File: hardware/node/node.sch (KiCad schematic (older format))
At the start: 66 parts, among them J1 BOOT0_Jumper, J2 FTDI, J3 SMA Female, J4 BATTERIES, J5 SWD, Q1 Si2323DDS, SW1 TVCM04N016BB, U1 RFM69HCW, U2 SHTC3, U3 AT25DF512C, U4 STM32L031K6Tx, U5 SN74LVC1T45DBV, U6 SN74LVC1T45DBV, Y1 32.768K-CFPX217

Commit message: Removed UART level translation
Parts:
- removed C10, C11, C8, C9: 100n, Capacitor_SMD:C_0805_2012Metric_Pad1.15x1.40mm_HandSolder, symbol Device:C
- removed R22, R27: 0, Resistor_SMD:R_0805_2012Metric_Pad1.15x1.40mm_HandSolder, symbol Device:R
- removed R23, R24, R26: 100k, Resistor_SMD:R_0805_2012Metric_Pad1.15x1.40mm_HandSolder, symbol Device:R
- removed R28, R29: 330, Resistor_SMD:R_0805_2012Metric_Pad1.15x1.40mm_HandSolder, symbol Device:R
- removed U5, U6: SN74LVC1T45DBV, Package_TO_SOT_SMD:SOT-23-6, symbol Logic_LevelTranslator:SN74LVC1T45DBV
- R11, R12, R14, R16: value 0 -> 330
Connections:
- net labels removed: FTDI_RX, FTDI_TX, FTDI_VCC
- wire segments 310 -> 248
- no-connect marks 9 -> 10
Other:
- note added: "FT232R (used in FTDI cable)\nhas a input switching voltage \nof max 1.5V so it should be \nfine to drive it directly at \neg 2.4 V"
- note added: "PA3 (USART2_RX) is 5V tolerant\nso it should be safe to connect\nit directly to 3.3V FTDI cable"
- note added: "Populate only\none set of \nresistors"
- note removed: "FT232R (used in FTDI cable) has a input switching voltage of max 1.5V\nso it should be fine to drive it directly at eg 2.4 V"
- note removed: "PA3 (USART2_RX) is 5V tolerant so it should \nbe safe to bypass level conversion"
- note removed: "Populate only\none set of resistors"
- note removed: "Power-off leakage current 2uA max"
- note removed: "UART level translation"

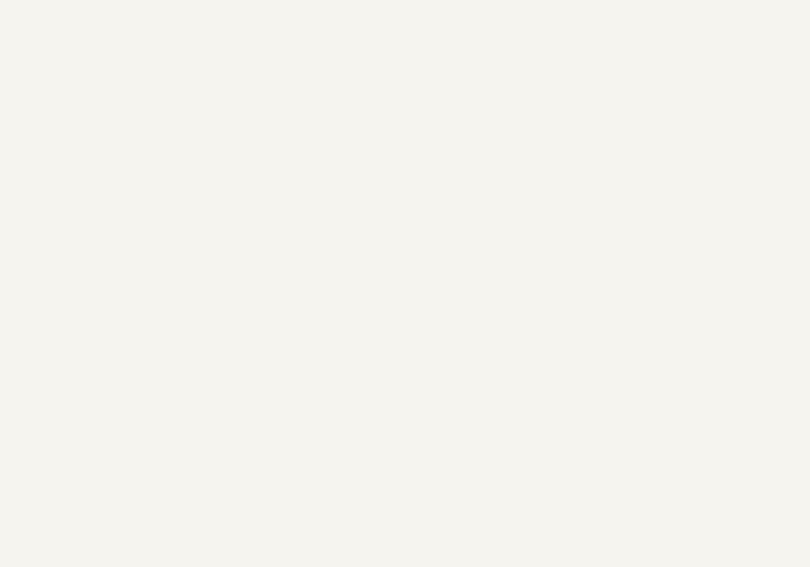
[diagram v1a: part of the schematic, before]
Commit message: Added 4 x M3 mounting holes
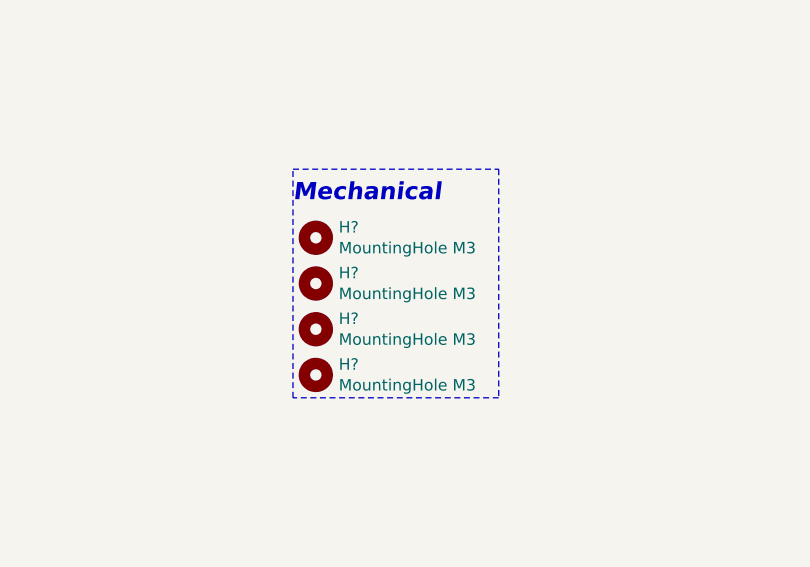
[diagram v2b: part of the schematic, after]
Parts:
- added H? (x4): MountingHole M3, MountingHole:MountingHole_3.2mm_M3, symbol Mechanical:MountingHole
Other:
- note added: "Mechanical"
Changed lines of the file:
@@
 Wire Notes Line
 	9450 3750 9450 500
+$Comp
+L Mechanical:MountingHole H?
+U 1 1 5E031363
+P 8850 4950
+F 0 "H?" H 8950 4996 50  0000 L CNN
+F 1 "MountingHole M3" H 8950 4905 50  0000 L CNN
+F 2 "MountingHole:MountingHole_3.2mm_M3" H 8850 4950 50  0001 C CNN
+F 3 "~" H 8850 4950 50  0001 C CNN
+	1    8850 4950
+	1    0    0    -1
+$EndComp
+$Comp
+L Mechanical:MountingHole H?
+U 1 1 5E031864
+P 8850 5150
+F 0 "H?" H 8950 5196 50  0000 L CNN
+F 1 "MountingHole M3" H 8950 5105 50  0000 L CNN
+F 2 "MountingHole:MountingHole_3.2mm_M3" H 8850 5150 50  0001 C CNN
+F 3 "~" H 8850 5150 50  0001 C CNN
+	1    8850 5150
+	1    0    0    -1
+$EndComp
+$Comp
+L Mechanical:MountingHole H?
+U 1 1 5E0318E6
+P 8850 5350
+F 0 "H?" H 8950 5396 50  0000 L CNN
+F 1 "MountingHole M3" H 8950 5305 50  0000 L CNN
+F 2 "MountingHole:MountingHole_3.2mm_M3" H 8850 5350 50  0001 C CNN
+F 3 "~" H 8850 5350 50  0001 C CNN
+	1    8850 5350
+	1    0    0    -1
+$EndComp
+$Comp
+L Mechanical:MountingHole H?
+U 1 1 5E03196A
+P 8850 5550
+F 0 "H?" H 8950 5596 50  0000 L CNN
+F 1 "MountingHole M3" H 8950 5505 50  0000 L CNN
+F 2 "MountingHole:MountingHole_3.2mm_M3" H 8850 5550 50  0001 C CNN
+F 3 "~" H 8850 5550 50  0001 C CNN
+	1    8850 5550
+	1    0    0    -1
+$EndComp
+Text Notes 8750 4800 0    75   Italic 15
+Mechanical
+Wire Notes Line
+	8750 4650 9650 4650
+Wire Notes Line
+	9650 4650 9650 5650
+Wire Notes Line
+	9650 5650 8750 5650
+Wire Notes Line
+	8750 5650 8750 4650
 $EndSCHEMATC

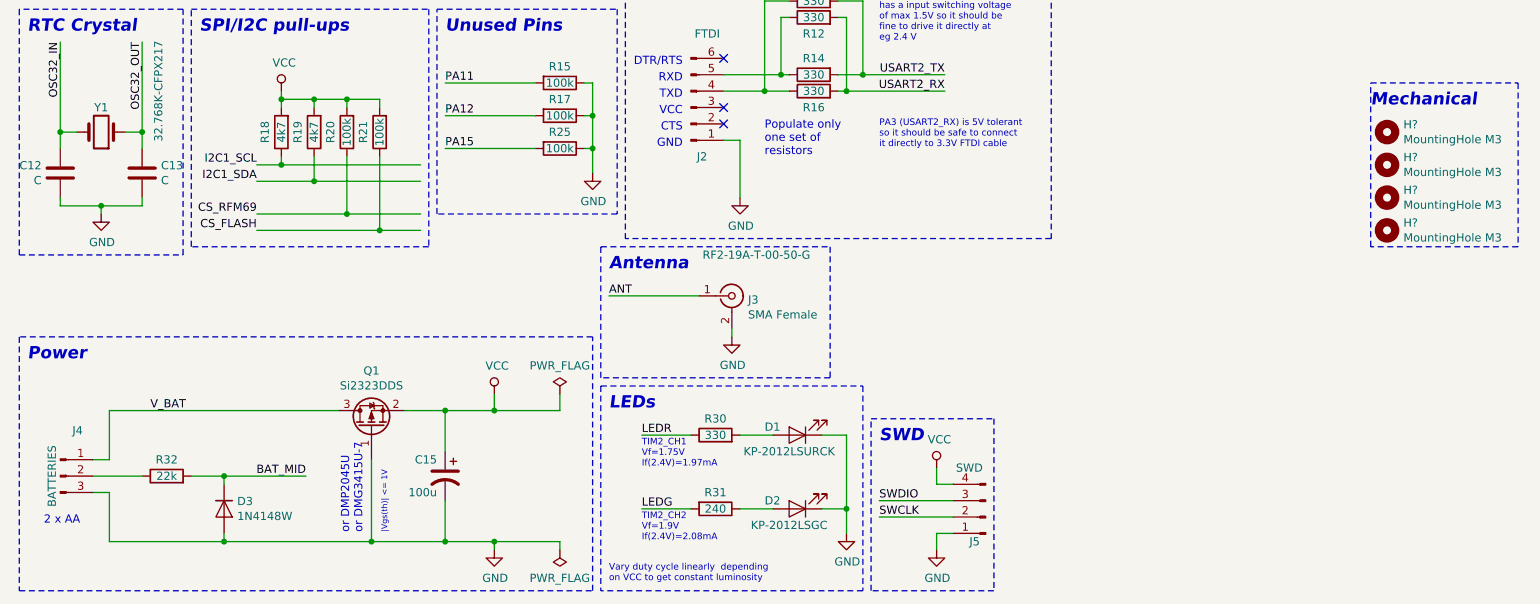
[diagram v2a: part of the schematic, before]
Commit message: PCB mount battery holders
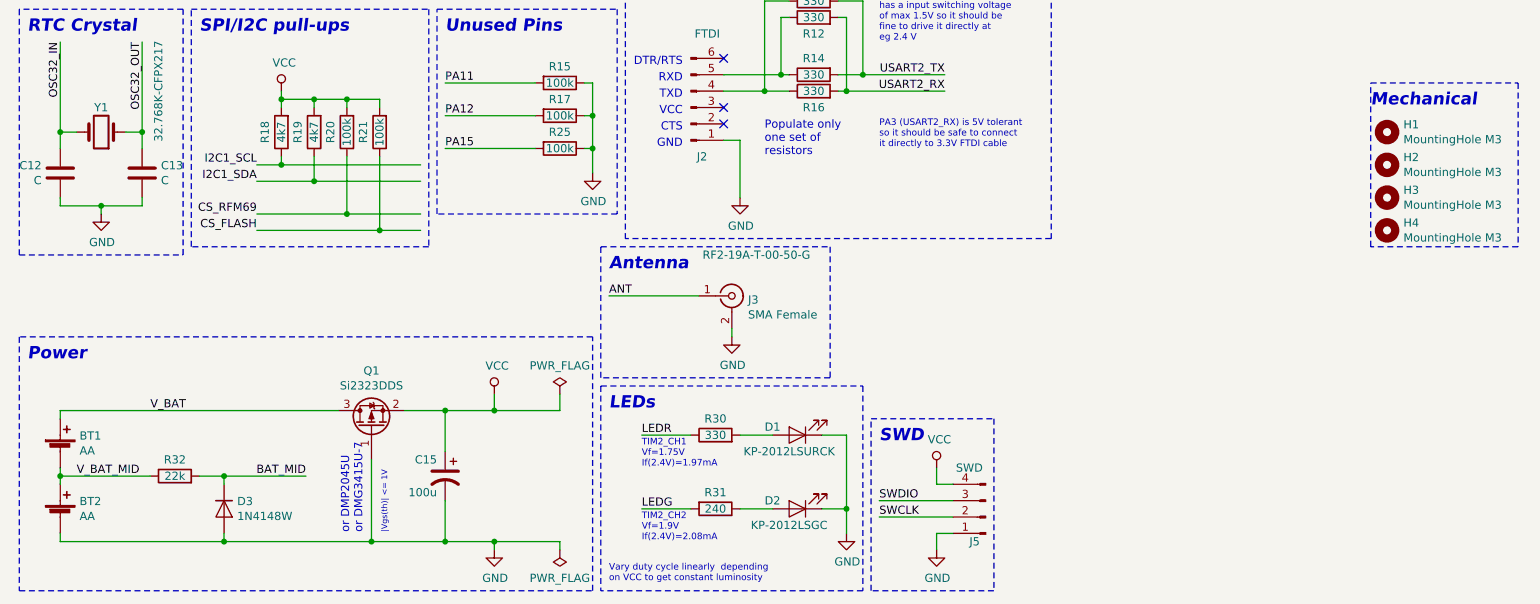
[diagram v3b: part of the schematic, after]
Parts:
- removed J4: BATTERIES, Connector_PinHeader_2.54mm:PinHeader_1x03_P2.54mm_Vertical, symbol Connector:Conn_01x03_Male
- added BT1, BT2: AA, humidity:AA_Battery_Holder, symbol Device:Battery_Cell
- gave numbers to parts that had none: 4
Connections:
- net GND: now also BT2.2 (-)
- net V_BAT: now also BT1.1 (+)
- net V_BAT_MID: now reaches R32.1
- net V_BAT_MID: now also BT1.2 (-), BT2.1 (+)
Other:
- note removed: "2 x AA"
- moved on the sheet: R32
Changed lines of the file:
@@
 Connect unused IO with a pull-up/down
-$Comp
-L Connector:Conn_01x03_Male J4
-U 1 1 5CDE51C7
-P 750 7050
-F 0 "J4" H 856 7328 50  0000 C CNN
-F 1 "BATTERIES" V 700 7050 50  0000 C CNN
-F 2 "Connector_PinHeader_2.54mm:PinHeader_1x03_P2.54mm_Vertical" H 750 7050 50  0001 C CNN
-F 3 "~" H 750 7050 50  0001 C CNN
-	1    750  7050
-	1    0    0    -1
-$EndComp
-Wire Wire Line
-	950  6950 1050 6950
-Wire Wire Line
-	1050 6650 1050 6950
-Wire Wire Line
-	950  7150 1050 7150
-Wire Wire Line
-	1050 7150 1050 7450
 $Comp
 L Device:Q_PMOS_GSD Q1
@@
 	2650 6950 2650 7450
 Wire Wire Line
-	1050 7450 1750 7450
-Wire Wire Line
 	2850 6650 3100 6650
 Wire Wire Line
@@
 Text Notes 2750 7400 1    35   ~ 0
 |Vgs(th)| <= 1V
-Text Notes 650  7350 0    50   ~ 0
-2 x AA
 Wire Wire Line
 	2150 3200 2750 3200
@@
 	4100 900  3900 900
 Wire Wire Line
-	950  7050 1250 7050
-Wire Wire Line
 	2250 7050 1750 7050
 Wire Wire Line
@@
 Connection ~ 1750 7050
 Wire Wire Line
-	1750 7050 1550 7050
+	1750 7050 1600 7050
 Wire Wire Line
 	1750 7400 1750 7450
@@
 L Device:R R32
 U 1 1 5D265FEC
-P 1400 7050
-F 0 "R32" V 1500 7050 50  0000 C CNN
-F 1 "22k" V 1400 7050 50  0000 C CNN
-F 2 "Resistor_SMD:R_0805_2012Metric_Pad1.15x1.40mm_HandSolder" V 1330 7050 50  0001 C CNN
-F 3 "~" H 1400 7050 50  0001 C CNN
-	1    1400 7050
-	0    -1   -1   0
-$EndComp
-Wire Wire Line
-	1050 6650 2450 6650
+P 1450 7050
+F 0 "R32" V 1550 7050 50  0000 C CNN
+F 1 "22k" V 1450 7050 50  0000 C CNN
+F 2 "Resistor_SMD:R_0805_2012Metric_Pad1.15x1.40mm_HandSolder" V 1380 7050 50  0001 C CNN
+F 3 "~" H 1450 7050 50  0001 C CNN
+	1    1450 7050
+	0    -1   -1   0
+$EndComp
 Wire Wire Line
 	1550 750  1550 850
@@
 	9450 3750 9450 500
 $Comp
-L Mechanical:MountingHole H?
+L Mechanical:MountingHole H1
 U 1 1 5E031363
 P 8850 4950
-F 0 "H?" H 8950 4996 50  0000 L CNN
+F 0 "H1" H 8950 4996 50  0000 L CNN
 F 1 "MountingHole M3" H 8950 4905 50  0000 L CNN
 F 2 "MountingHole:MountingHole_3.2mm_M3" H 8850 4950 50  0001 C CNN
@@
 $EndComp
 $Comp
-L Mechanical:MountingHole H?
+L Mechanical:MountingHole H2
 U 1 1 5E031864
 P 8850 5150
-F 0 "H?" H 8950 5196 50  0000 L CNN
+F 0 "H2" H 8950 5196 50  0000 L CNN
 F 1 "MountingHole M3" H 8950 5105 50  0000 L CNN
 F 2 "MountingHole:MountingHole_3.2mm_M3" H 8850 5150 50  0001 C CNN
@@
 $EndComp
 $Comp
-L Mechanical:MountingHole H?
+L Mechanical:MountingHole H3
 U 1 1 5E0318E6
 P 8850 5350
-F 0 "H?" H 8950 5396 50  0000 L CNN
+F 0 "H3" H 8950 5396 50  0000 L CNN
 F 1 "MountingHole M3" H 8950 5305 50  0000 L CNN
 F 2 "MountingHole:MountingHole_3.2mm_M3" H 8850 5350 50  0001 C CNN
@@
 $EndComp
 $Comp
-L Mechanical:MountingHole H?
+L Mechanical:MountingHole H4
 U 1 1 5E03196A
 P 8850 5550
-F 0 "H?" H 8950 5596 50  0000 L CNN
+F 0 "H4" H 8950 5596 50  0000 L CNN
 F 1 "MountingHole M3" H 8950 5505 50  0000 L CNN
 F 2 "MountingHole:MountingHole_3.2mm_M3" H 8850 5550 50  0001 C CNN
@@
 Wire Notes Line
 	8750 5650 8750 4650
+$Comp
+L Device:Battery_Cell BT1
+U 1 1 5E042F5F
+P 750 6900
+F 0 "BT1" H 868 6996 50  0000 L CNN
+F 1 "AA" H 868 6905 50  0000 L CNN
+F 2 "humidity:AA_Battery_Holder" V 750 6960 50  0001 C CNN
+F 3 "https://www.electrokit.com/produkt/batterihallare-1xaa-pcb/" V 750 6960 50  0001 C CNN
+F 4 "electrokit: 41003559" H 750 6900 50  0001 C CNN "Part"
+	1    750  6900
+	1    0    0    -1
+$EndComp
+Wire Wire Line
+	750  6650 750  6700
+Wire Wire Line
+	750  6650 2450 6650
+Wire Wire Line
+	750  7100 750  7050
+Wire Wire Line
+	750  7050 1300 7050
+Connection ~ 750  7050
+Wire Wire Line
+	750  7050 750  7000
+Wire Wire Line
+	750  7450 750  7400
+Wire Wire Line
+	750  7450 1750 7450
+$Comp
+L Device:Battery_Cell BT2
+U 1 1 5E0BA08E
+P 750 7300
+F 0 "BT2" H 868 7396 50  0000 L CNN
+F 1 "AA" H 868 7305 50  0000 L CNN
+F 2 "humidity:AA_Battery_Holder" V 750 7360 50  0001 C CNN
+F 3 "https://www.electrokit.com/produkt/batterihallare-1xaa-pcb/" V 750 7360 50  0001 C CNN
+F 4 "electrokit: 41003559" H 750 7300 50  0001 C CNN "Part"
+	1    750  7300
+	1    0    0    -1
+$EndComp
+Text Label 850  7050 0    50   ~ 0
+V_BAT_MID
 $EndSCHEMATC

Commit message: First layout
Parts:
- C1, C12, C13, C14, C2, C3, C4, C6, C7: footprint Capacitor_SMD:C_0805_2012Metric_Pad1.15x1.40mm_HandSolder -> Capacitor_SMD:C_0603_1608Metric_Pad1.05x0.95mm_HandSolder
- J1: footprint Connector_PinHeader_2.54mm:PinHeader_1x02_P2.54mm_Vertical -> Connector_PinHeader_2.54mm:PinHeader_1x02_P2.54mm_Horizontal
- J2: footprint Connector_PinHeader_2.54mm:PinHeader_1x06_P2.54mm_Vertical -> Connector_PinHeader_2.54mm:PinHeader_1x06_P2.54mm_Horizontal
- J5: footprint Connector_PinHeader_2.54mm:PinHeader_1x04_P2.54mm_Vertical -> Connector_PinHeader_2.54mm:PinHeader_1x04_P2.54mm_Horizontal
- R1, R10, R11, R12, R13, R14, R15, R16, R17, R18, R19, R2, R20, R21, R25, R3, R30, R31, R32, R33, R34, R4, R5, R6, R7, R8, R9: footprint Resistor_SMD:R_0805_2012Metric_Pad1.15x1.40mm_HandSolder -> Resistor_SMD:R_0603_1608Metric_Pad1.05x0.95mm_HandSolder
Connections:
- net CS_FLASH: now also U4.14 (PB0); no longer U4.15 (PB1)
- net CS_RFM69: now also U4.15 (PB1); no longer U4.14 (PB0)
- net GND: no longer J2.1 (Pin_1)
- net FTDI_TX: now reaches J2.4 (Pin_4), R11.1, R16.1
- net FTDI_RX: now reaches J2.5 (Pin_5), R12.1, R14.1
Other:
- moved on the sheet: R11, R12, R14, R16

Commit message: PCB with batteries
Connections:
- net GND: now also J2.1 (Pin_1)
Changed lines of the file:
@@
 L power:GND #PWR029
 U 1 1 5CF5D50D
-P 5200 5350
-F 0 "#PWR029" H 5200 5100 50  0001 C CNN
-F 1 "GND" H 5205 5177 50  0000 C CNN
-F 2 "" H 5200 5350 50  0001 C CNN
-F 3 "" H 5200 5350 50  0001 C CNN
-	1    5200 5350
+P 4900 5350
+F 0 "#PWR029" H 4900 5100 50  0001 C CNN
+F 1 "GND" H 4905 5177 50  0000 C CNN
+F 2 "" H 4900 5350 50  0001 C CNN
+F 3 "" H 4900 5350 50  0001 C CNN
+	1    4900 5350
 	1    0    0    -1
 $EndComp
